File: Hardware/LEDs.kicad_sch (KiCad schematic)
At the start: 17 parts, among them U8 PCA9685BS

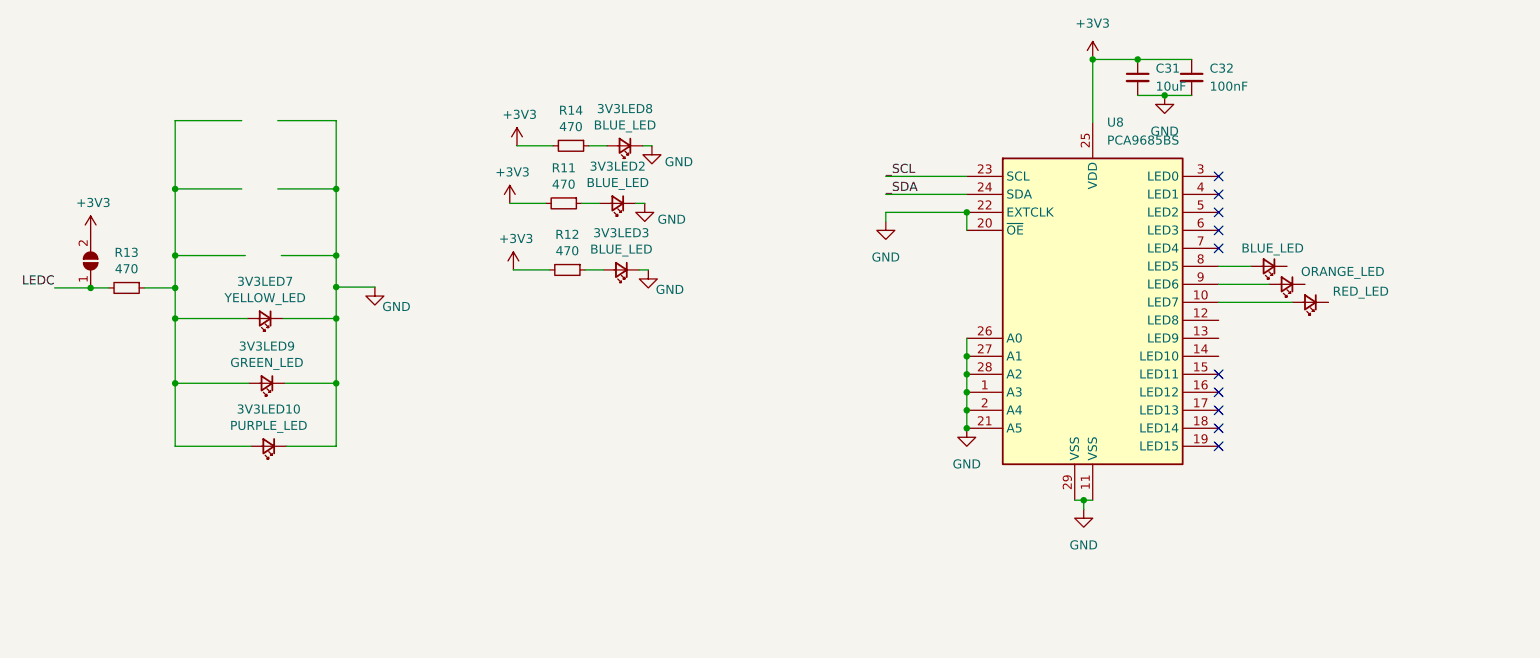
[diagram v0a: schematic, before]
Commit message: Finished Boosts and Sensors
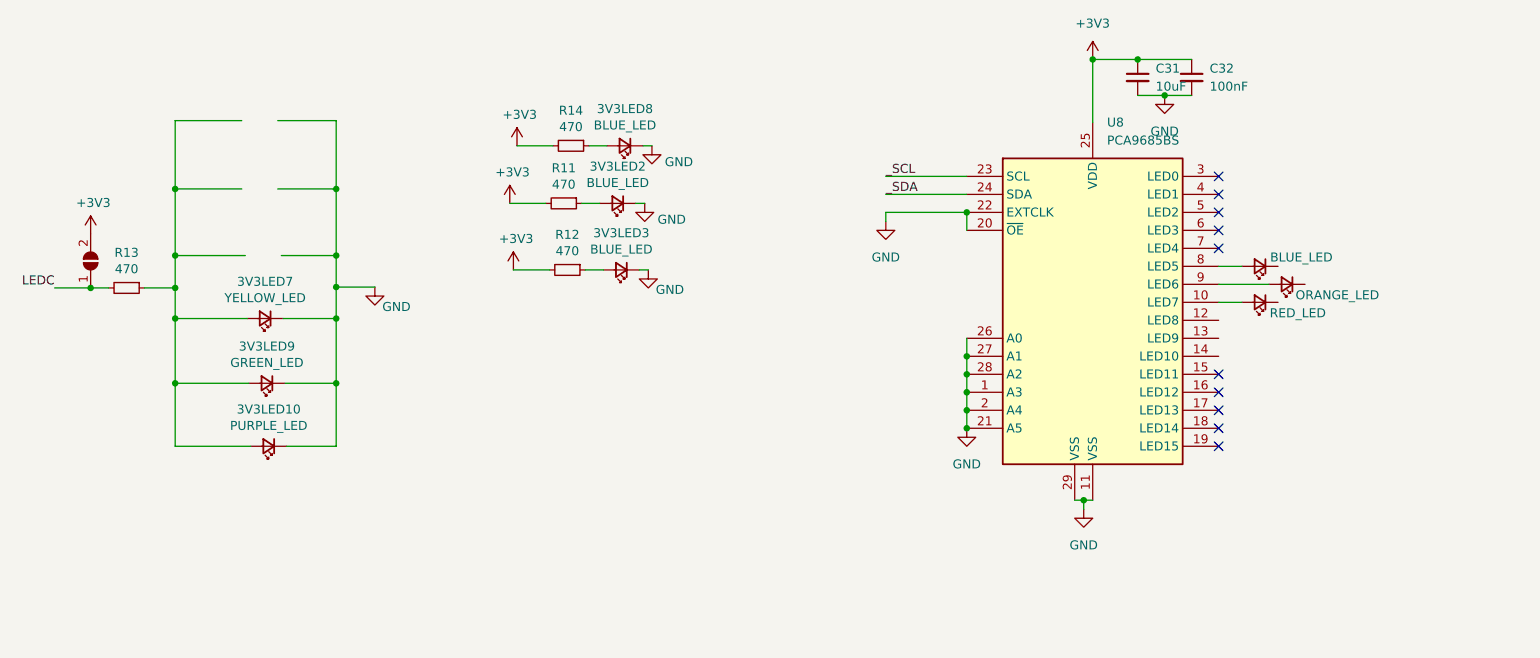
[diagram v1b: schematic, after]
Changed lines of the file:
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@@
 (kicad_sch
-	(version 20231120)
+	(version 20250114)
 	(generator "eeschema")
-	(generator_version "8.0")
+	(generator_version "9.0")
 	(paper "A4")
 	(junction
@@
 	(wire
 		(pts
-			(xy 221.742 85.852) (xy 211.328 85.852)
+			(xy 214.63 85.852) (xy 211.328 85.852)
 		)
 		(stroke
@@
 	(wire
 		(pts
-			(xy 215.9 80.772) (xy 211.328 80.772)
+			(xy 214.63 80.772) (xy 211.328 80.772)
 		)
 		(stroke
@@
 	(label "LEDC"
 		(at 46.99 83.82 180)
-		(fields_autoplaced yes)
 		(effects
 			(font
@@
 	(label "_SCL"
 		(at 164.338 68.072 0)
-		(fields_autoplaced yes)
 		(effects
 			(font
@@
 	(label "_SDA"
 		(at 164.338 70.612 0)
-		(fields_autoplaced yes)
 		(effects
 			(font
@@
 		)
 		(property "Value" "ORANGE_LED"
-			(at 228.854 81.534 0)
+			(at 228.092 84.836 0)
 			(effects
 				(font
@@
 	(symbol
 		(lib_id "Device:LED_Small")
-		(at 224.282 85.852 180)
+		(at 217.17 85.852 180)
 		(unit 1)
 		(exclude_from_sim no)
@@
 		(dnp no)
 		(property "Reference" "3V3LED6"
-			(at 224.282 80.645 0)
+			(at 217.17 80.645 0)
 			(effects
 				(font
@@
 		)
 		(property "Value" "RED_LED"
-			(at 231.394 84.328 0)
+			(at 222.504 87.376 0)
 			(effects
 				(font
@@
 		)
 		(property "Footprint" "LED_SMD:LED_0402_1005Metric"
-			(at 224.282 85.852 90)
+			(at 217.17 85.852 90)
 			(effects
 				(font
@@
 		)
 		(property "Datasheet" "~"
-			(at 224.282 85.852 90)
+			(at 217.17 85.852 90)
 			(effects
 				(font
@@
 		)
 		(property "Description" ""
-			(at 224.282 85.852 0)
+			(at 217.17 85.852 0)
 			(effects
 				(font
@@
 	(symbol
 		(lib_id "Device:LED_Small")
-		(at 218.44 80.772 180)
+		(at 217.17 80.772 180)
 		(unit 1)
 		(exclude_from_sim no)
@@
 		(dnp no)
 		(property "Reference" "3V3LED4"
-			(at 218.44 75.565 0)
+			(at 217.17 75.565 0)
 			(effects
 				(font
@@
 		)
 		(property "Value" "BLUE_LED"
-			(at 218.948 78.232 0)
+			(at 223.012 79.502 0)
 			(effects
 				(font
@@
 		)
 		(property "Footprint" "LED_SMD:LED_0402_1005Metric"
-			(at 218.44 80.772 90)
+			(at 217.17 80.772 90)
 			(effects
 				(font
@@
 		)
 		(property "Datasheet" "~"
-			(at 218.44 80.772 90)
+			(at 217.17 80.772 90)
 			(effects
 				(font
@@
 		)
 		(property "Description" ""
-			(at 218.44 80.772 0)
-			(effects
-				(font
+			(at 217.17 80.772 0)
+			(effects
+				(font

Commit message: Routed Switch and Servo driver subsystems
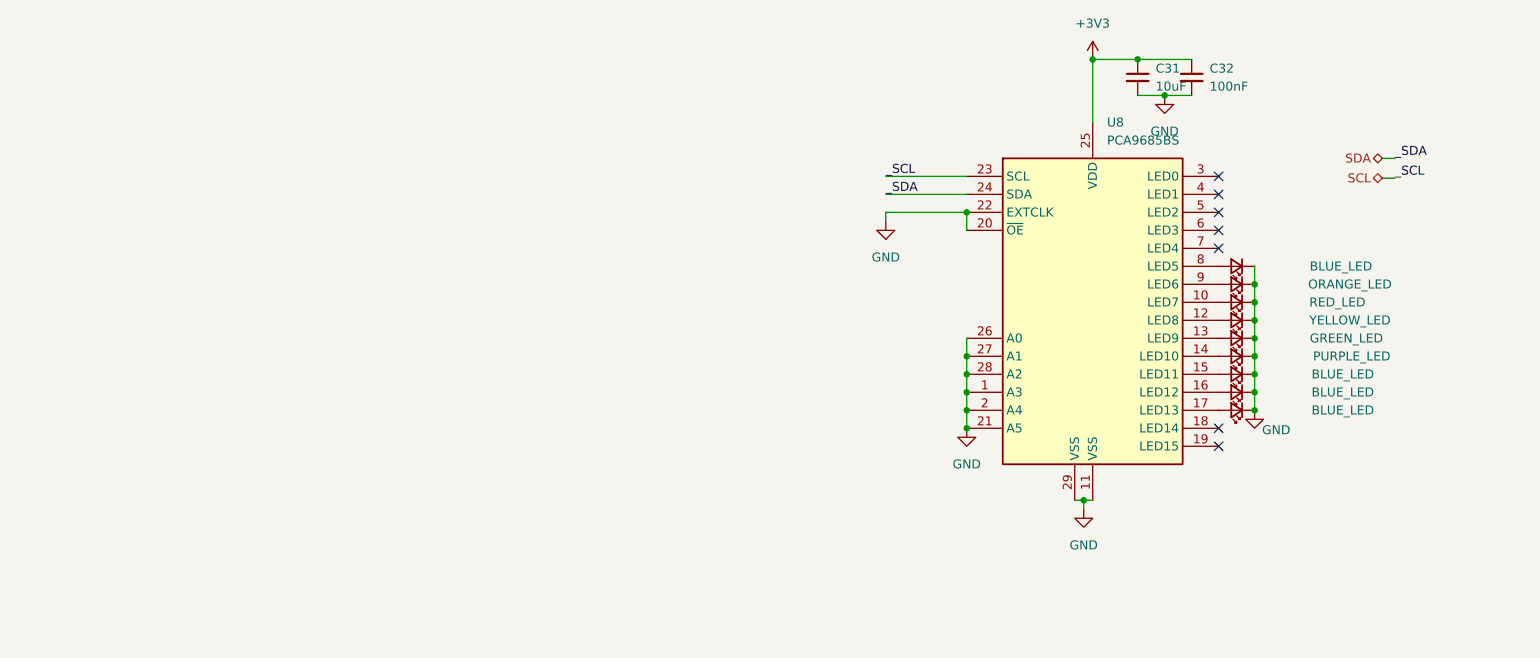
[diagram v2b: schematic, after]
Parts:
- removed JP2: SolderJumper_2_Open, iclr:SmallerSolderJP, symbol Jumper:SolderJumper_2_Open
- removed R11, R12, R13, R14: 470, Resistor_SMD:R_0402_1005Metric, symbol Device:R_Small
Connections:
- net GND: now also 3V3LED4.1 (K), 3V3LED5.1 (K), 3V3LED6.1 (K)
- net at 3V3LED2.2 (A): now also U8.16 (LED12)
- net at 3V3LED8.2 (A): now also U8.15 (LED11)
- net at 3V3LED3.2 (A): now also U8.17 (LED13)
- net at U8.12 (LED8): now also 3V3LED7.2 (A)
- net at U8.13 (LED9): now also 3V3LED9.2 (A)
- net at U8.14 (LED10): now also 3V3LED10.2 (A)
- net _SCL renamed SCL
- net _SDA renamed SDA
- no-connect marks 10 -> 7

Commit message: Added actuators and I2C bus
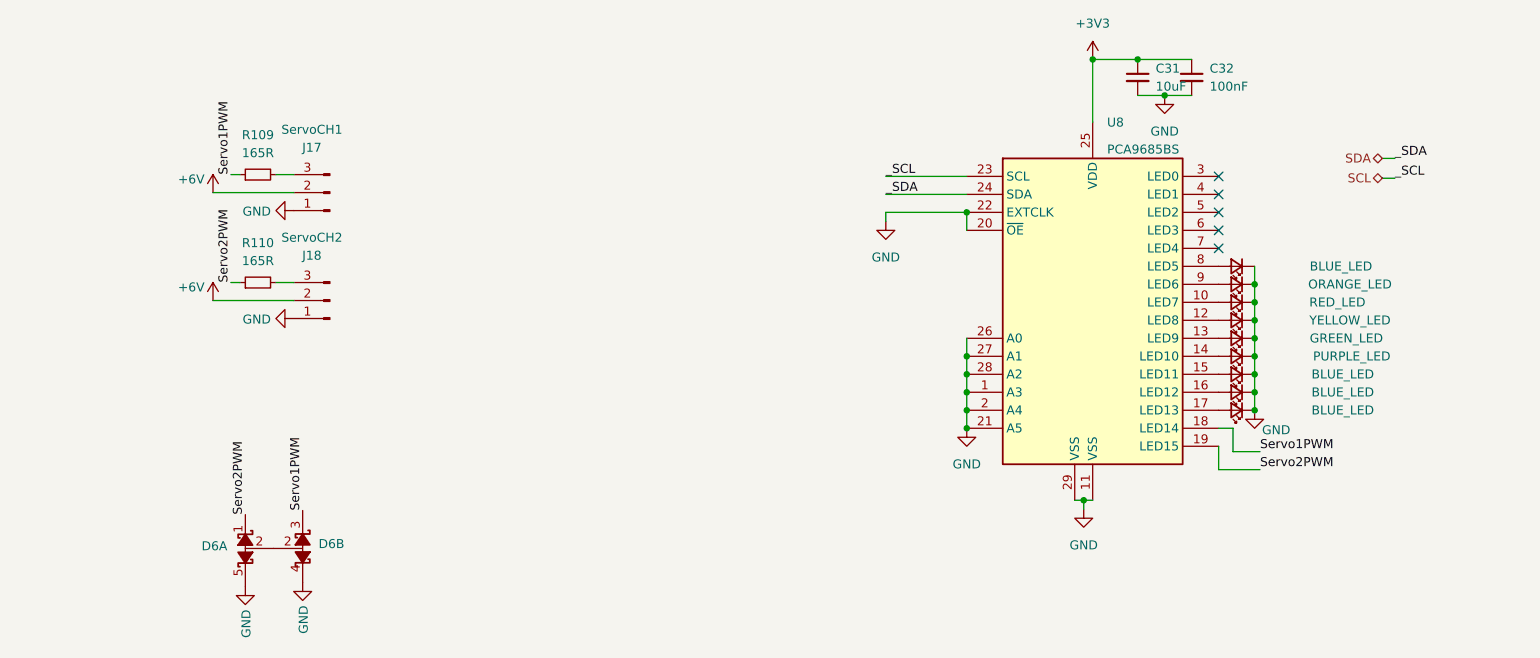
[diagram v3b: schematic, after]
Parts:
- added D6: ~, Package_TO_SOT_SMD:SOT-353_SC-70-5, symbol iclr:CPDV5-3V3UP
- added J17: ServoCH1, Connector_Molex:Molex_Nano-Fit_105313-xx03_1x03_P2.50mm_Horizontal, symbol Connector:Conn_01x03_Male
- added J18: ServoCH2, Connector_Molex:Molex_Nano-Fit_105313-xx03_1x03_P2.50mm_Horizontal, symbol Connector:Conn_01x03_Male
- added R109, R110: 165R, Resistor_SMD:R_0402_1005Metric, symbol Device:R_Small
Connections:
- net GND: now also D6.4, D6.5, J17.1 (Pin_1), J18.1 (Pin_1)
- net Servo1PWM: now reaches U8.18 (LED14)
- net Servo1PWM: now also D6.3, R109.1
- net Servo2PWM: now reaches U8.19 (LED15)
- net Servo2PWM: now also D6.1, R110.1
- new net: J17.3 (Pin_3), R109.2
- new net: D6.2, D6.2
- new net: J18.3 (Pin_3), R110.2
- new net +6V: J17.2 (Pin_2), J18.2 (Pin_2)
- no-connect marks 7 -> 5

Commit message: Almost done
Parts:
- removed 3V3LED2, 3V3LED3: BLUE_LED, LED_SMD:LED_0402_1005Metric, symbol Device:LED_Small
- removed 3V3LED9: GREEN_LED, LED_SMD:LED_0402_1005Metric, symbol Device:LED_Small
- added R12: 470, Resistor_SMD:R_0402_1005Metric, symbol Device:R_Small
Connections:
- net +3V3: now also R12.2
- net at 3V3LED5.2 (A): now also U8.4 (LED1); no longer U8.9 (LED6)
- net at 3V3LED10.2 (A): now also U8.8 (LED5); no longer U8.14 (LED10)
- net at 3V3LED6.2 (A): now also U8.5 (LED2); no longer U8.10 (LED7)
- net at 3V3LED4.2 (A): now also U8.7 (LED4); no longer U8.8 (LED5)
- net at 3V3LED7.2 (A): now also U8.6 (LED3); no longer U8.12 (LED8)
- net at 3V3LED8.2 (A): now also R12.1; no longer U8.15 (LED11)
- removed net Servo1PWM: D6.3, R109.1, U8.18 (LED14)
- removed net Servo2PWM: D6.1, R110.1, U8.19 (LED15)
- new net Servo0: D6.1, R109.1
- new net Servo1: R110.1
- no-connect marks 5 -> 1
